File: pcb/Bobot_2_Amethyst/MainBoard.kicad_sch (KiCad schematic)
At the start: 6 parts, among them J1 Conn_01x04_Socket, J5 Conn_01x05_Socket, J6 Conn_01x05_Socket, U2 ESP32_DevKit_V1_DOIT

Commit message: pcb: complete BMS board schematic
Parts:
- R1, R2: footprint Resistor_SMD:R_0201_0603Metric -> Resistor_SMD:R_0805_2012Metric_Pad1.20x1.40mm_HandSolder
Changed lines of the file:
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@@
 			)
 		)
-		(property "Footprint" "Resistor_SMD:R_0201_0603Metric"
+		(property "Footprint" "Resistor_SMD:R_0805_2012Metric_Pad1.20x1.40mm_HandSolder"
 			(at 105.156 86.614 90)
 			(effects
@@
 			)
 		)
-		(property "Footprint" "Resistor_SMD:R_0201_0603Metric"
+		(property "Footprint" "Resistor_SMD:R_0805_2012Metric_Pad1.20x1.40mm_HandSolder"
 			(at 94.996 86.614 90)
 			(effects

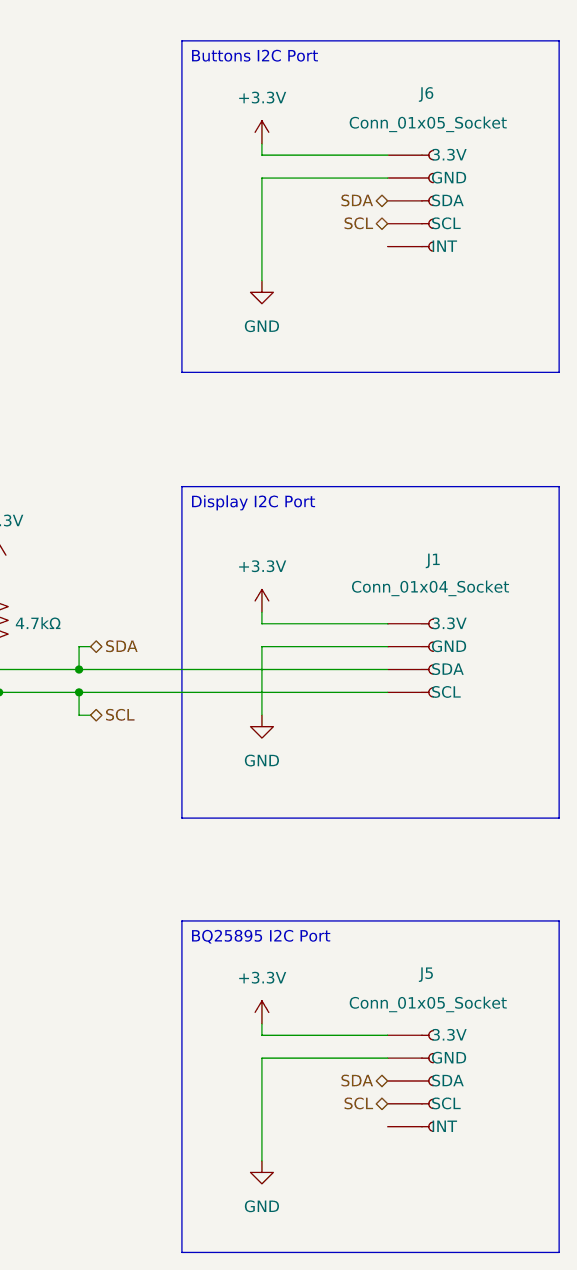
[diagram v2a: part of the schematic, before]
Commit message: pcb: add buttons board schematics except I2C address
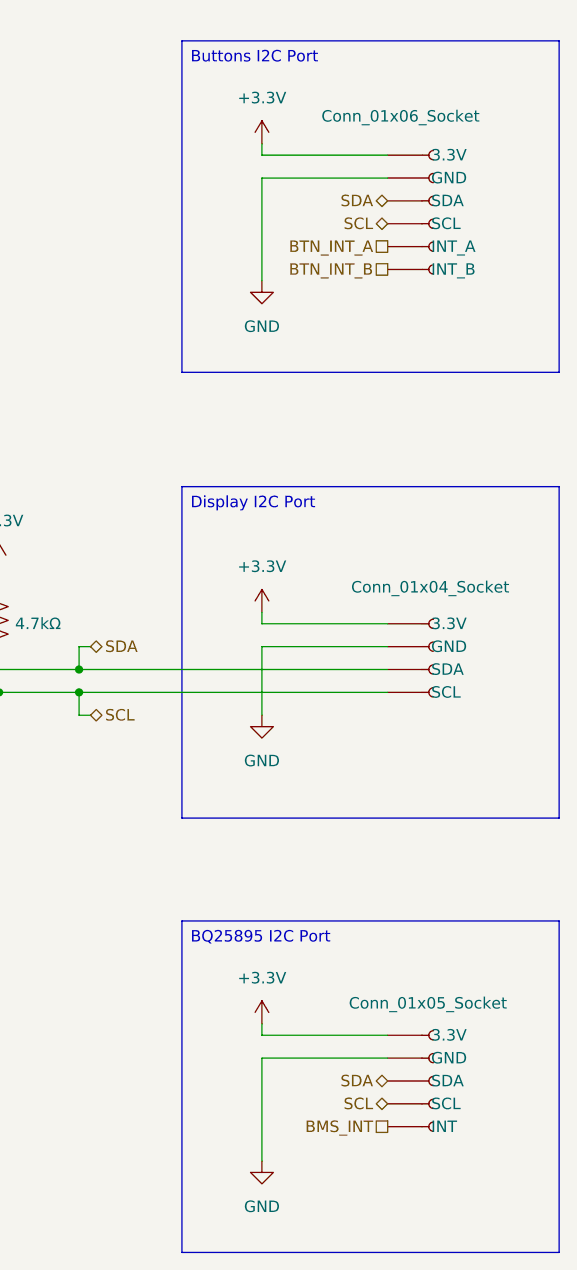
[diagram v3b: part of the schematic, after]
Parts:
- J6: value Conn_01x05_Socket -> Conn_01x06_Socket; footprint Connector_JST:JST_XH_B5B-XH-A_1x05_P2.50mm_Vertical -> Connector_JST:JST_XH_B6B-XH-A_1x06_P2.50mm_Vertical; symbol Connector:Conn_01x05_Socket -> Connector:Conn_01x06_Socket
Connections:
- net BTN_INT_A: now reaches J6.5 (INT_A)
- net BMS_INT: now reaches J5.5 (INT)
- new net BTN_INT_B: J6.6 (INT_B)
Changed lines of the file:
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@@
+		)
+	)
+	(hierarchical_label "BMS_INT"
+		(shape passive)
+		(at 147.32 142.24 180)
+		(effects
+			(font
+				(size 1.27 1.27)
+			)
+			(justify right)
 		)
 	)
@@
 		)
 	)
+	(hierarchical_label "BTN_INT_A"
+		(shape passive)
+		(at 147.32 44.45 180)
+		(effects
+			(font
+				(size 1.27 1.27)
+			)
+			(justify right)
+		)
+	)
 	(hierarchical_label "SDA"
 		(shape bidirectional)
@@
 		)
 	)
+	(hierarchical_label "BTN_INT_B"
+		(shape passive)
+		(at 147.32 46.99 180)
+		(effects
+			(font
+				(size 1.27 1.27)
+			)
+			(justify right)
+		)
+	)
 	(hierarchical_label "SDA"
 		(shape bidirectional)
@@
 	)
 	(symbol
-		(lib_id "Connector:Conn_01x05_Socket")
+		(lib_id "Connector:Conn_01x06_Socket")
 		(at 152.4 39.37 0)
 		(unit 1)
@@
 		(fields_autoplaced yes)
 		(property "Reference" "J6"
-			(at 150.876 27.432 0)
+			(at 153.67 39.3699 0)
 			(effects
 				(font
@@
 				)
 				(justify left)
-			)
-		)
-		(property "Value" "Conn_01x05_Socket"
-			(at 143.002 30.734 0)
+				(hide yes)
+			)
+		)
+		(property "Value" "Conn_01x06_Socket"
+			(at 139.954 29.972 0)
 			(effects
 				(font
@@
 			)
 		)
-		(property "Footprint" "Connector_JST:JST_XH_B5B-XH-A_1x05_P2.50mm_Vertical"
-			(at 152.4 13.97 0)
+		(property "Footprint" "Connector_JST:JST_XH_B6B-XH-A_1x06_P2.50mm_Vertical"
+			(at 152.146 24.638 0)
 			(effects
 				(font
@@
 			)
 		)
-		(property "Description" "Generic connector, single row, 01x05, script generated"
-			(at 152.654 20.32 0)
+		(property "Description" "Generic connector, single row, 01x06, script generated"
+			(at 151.638 19.304 0)
 			(effects
 				(font
@@
 		)
 		(pin "5"
+		)
+		(pin "6"
 		)
 		(instances
@@
 				)
 				(justify left)
+				(hide yes)
 			)
 		)
@@
 				)
 				(justify left)
-			)
-		)
+				(hide yes)
+			)
+		)

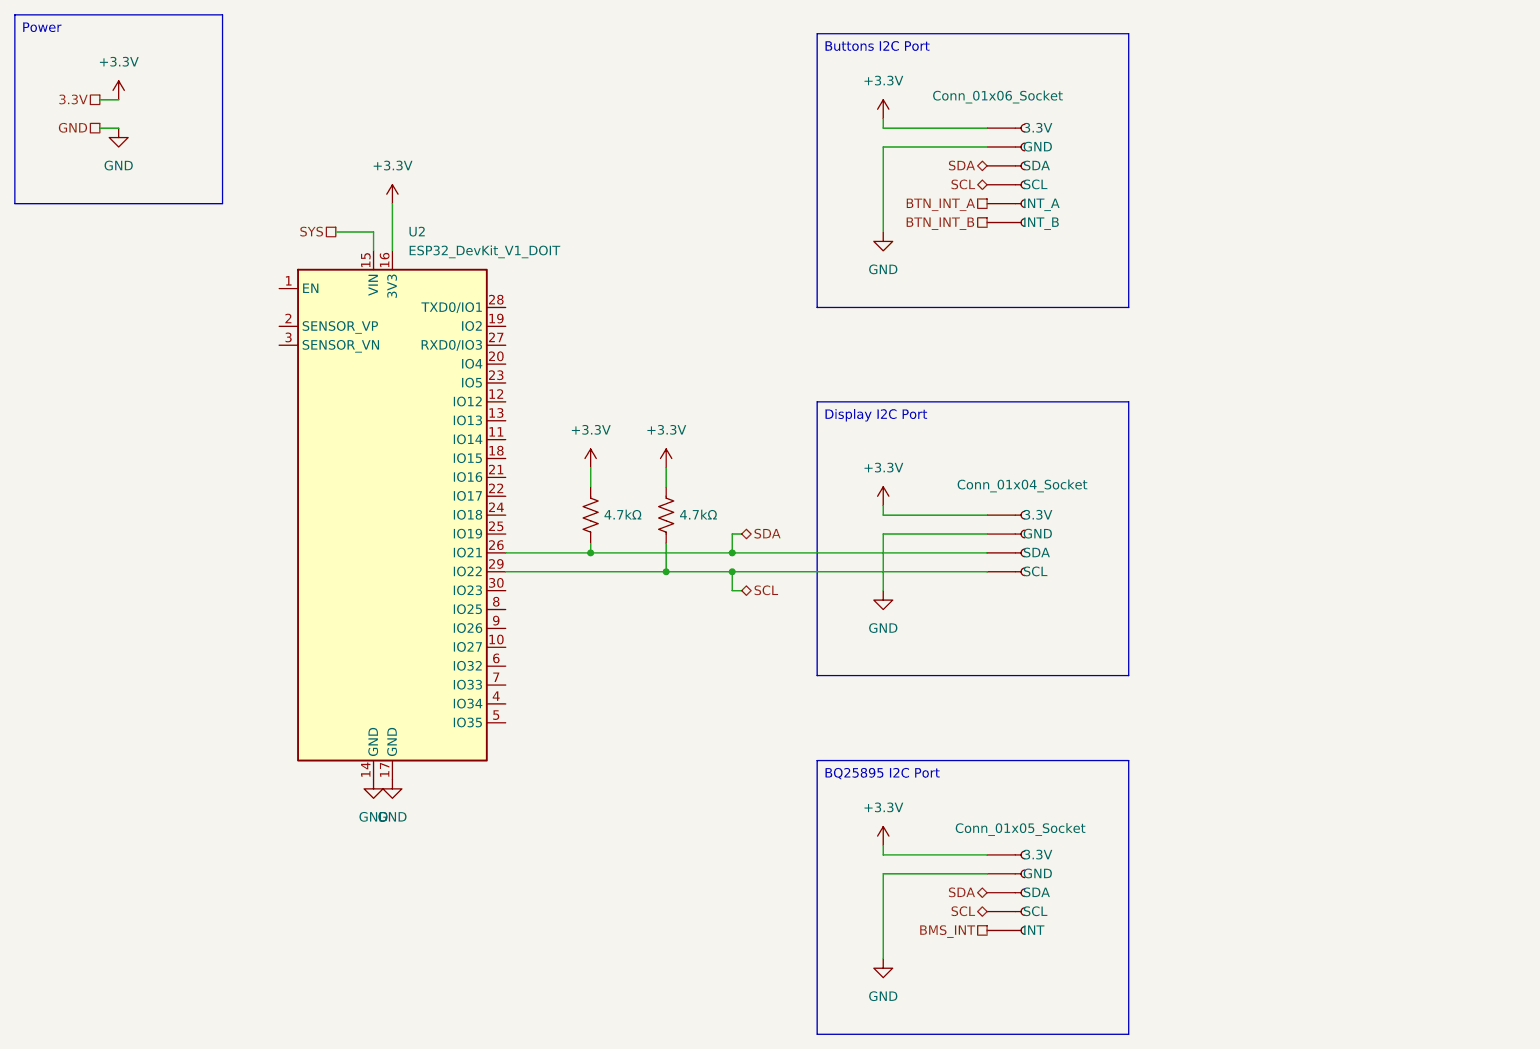
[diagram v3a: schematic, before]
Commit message: pcb: add touch sensor board
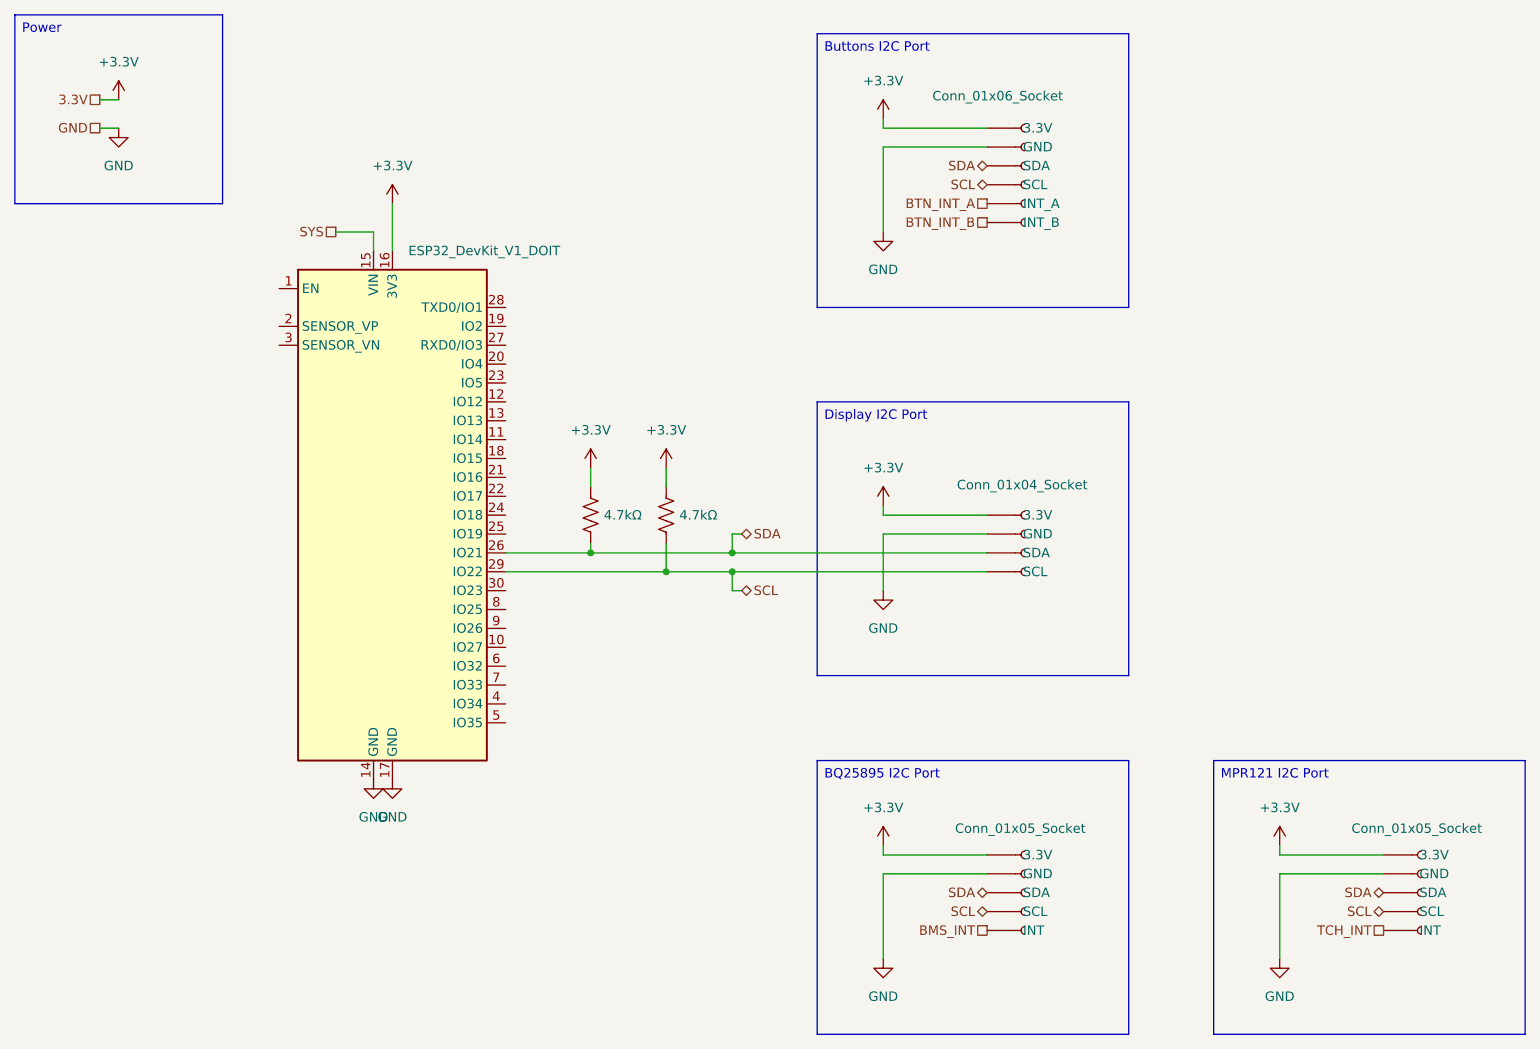
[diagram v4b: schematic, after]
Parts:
- added J9: Conn_01x05_Socket, Connector_JST:JST_XH_B5B-XH-A_1x05_P2.50mm_Vertical, symbol Connector:Conn_01x05_Socket
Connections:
- net +3.3V: now also J9.1 (3.3V)
- net GND: now also J9.2 (GND)
- net SCL: now also J9.4 (SCL)
- net SDA: now also J9.3 (SDA)
- new net TCH_INT: J9.5 (INT)
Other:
- title: (none) -> Main Board with ESP32
